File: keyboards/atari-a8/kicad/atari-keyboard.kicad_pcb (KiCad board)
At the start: 2 copper layers, 160 parts, among them J101 PLAYER 1, J102 PLAYER 2, J103 I2C DISPLAY, SW200 ESC, SW201 1, SW202 2, SW203 3, SW204 4, SW205 5, SW206 6, SW207 7, SW208 8, SW209 9, SW210 0, SW211 LT, SW212 GT, SW213 BS, SW214 C_UP, SW215 C_LEFT, SW216 C_DOWN, SW217 C_RIGHT, SW218 TAB, SW219 Q, SW220 W, SW221 E, SW222 R, SW223 T, SW224 Y, SW225 U, SW226 I, SW227 O, SW228 P, SW229 DASH, SW230 EQUAL, SW231 RETURN, SW232 HELP, SW233 RESET, SW234 OPTION, SW235 SELECT, SW236 CONTROL, SW237 A, SW238 S, SW239 D, SW240 F, SW241 G, SW242 H, SW243 J, SW244 K, SW245 L, SW246 SEMI, SW247 PLUS, SW248 ASTRIX, SW249 CAPS, SW250 START, SW251 POWER, SW252 MENU, SW253 TURBO, SW254 FN, SW255 LSHIFT, SW256 Z, SW257 X, SW258 C, SW259 V, SW260 B, SW261 N, SW262 M, SW263 COMMA, SW264 PERIOD, SW265 SLASH, SW266 RSHIFT, SW267 INV, SW268 BREAK, SW269 SPACE, U101 Elite-C

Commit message: Correct key sizes placed, diodes located, various auto-drawn stuff removed from PCB
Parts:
- removed D106: JS2_UP, keebio:Diode-dual
- removed D107: JS2_TRIG, retro-kbd:Diode-dual
- removed D108: JS2_DOWN, retro-kbd:Diode-dual
- removed D109: JS2_LEFT, retro-kbd:Diode-dual
- removed D110: JS2_RIGHT, retro-kbd:Diode-dual
- removed J102: PLAYER 2, Connector_Dsub:DSUB-9_Male_Horizontal_P2.77x2.84mm_EdgePinOffset9.90mm_Housed_MountingHolesOffset11.32mm
- SW200, SW232, SW233, SW234, SW235, SW249, SW250, SW251, SW252, SW253, SW267, SW268: footprint mx_alps:MX-1U -> mx_alps:MX-1.25U
- SW213, SW236: footprint mx_alps:MX-1U -> mx_alps:MX-2U
- SW218, SW266: footprint mx_alps:MX-1U -> mx_alps:MX-1.75U
- SW231: footprint mx_alps:MX-1U -> mx_alps:MX-1.5U
- SW255: footprint mx_alps:MX-1U -> mx_alps:MX-2.25U
- SW269: footprint mx_alps:MX-1U -> mx_alps:MX-6.25U
- moved SW250 746.5 mm to (354.8, 273.8)
- moved SW217 738.3 mm to (328.6, 276.2)
- moved SW214 735.0 mm to (309.6, 257.2)
- moved SW235 729.6 mm to (354.8, 250.0)
- moved SW234 728.4 mm to (354.8, 226.2)
- moved SW216 727.2 mm to (309.6, 276.2)
- moved SW233 727.2 mm to (354.8, 202.4)
- moved SW232 724.4 mm to (354.8, 173.8)
- moved SW215 717.0 mm to (290.5, 276.2)
- moved SW213 712.8 mm to (300.0, 200.0)
- moved SW231 702.9 mm to (304.8, 219.1)
- moved SW212 693.4 mm to (271.5, 200.0)
- moved H104 693.4 mm to (371.2, 290.3)
- moved D250 692.8 mm to (364.3, 276.2), turned to -90 degrees
- moved SW230 690.6 mm to (281.0, 219.1)
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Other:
- board outline added: 357.2 x 140.5 mm

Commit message: 3d models properly placed
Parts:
- moved D269 50.0 mm to (238.1, 280.6)
- moved D255 12.1 mm to (76.2, 261.6)
- moved D236 9.73 mm to (66.7, 242.5)
- moved D213 9.73 mm to (319.1, 204.4)
- moved D266 7.42 mm to (300.0, 261.6)
- moved D218 7.42 mm to (61.9, 223.5)
- moved D231 5.17 mm to (319.1, 223.5)
- moved D200 3.11 mm to (52.4, 204.4)
- moved D251 3.11 mm to (114.3, 178.2)
- moved D252 3.11 mm to (152.4, 178.2)
- moved D253 3.11 mm to (176.2, 178.2)
- moved D232 3.11 mm to (366.7, 178.2)
- moved D233 3.11 mm to (366.7, 206.8)
- moved D234 3.11 mm to (366.7, 230.6)
- moved D235 3.11 mm to (366.7, 254.4)
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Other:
- outline, holes or cut-outs redrawn

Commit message: All global labels rendered. MAX7219's added. PCB updaed
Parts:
- added C101: 47uF, Capacitor_THT:CP_Radial_D5.0mm_P2.50mm, F.Cu at (210.0, 173.0)
- added C102: 0.1uF, Capacitor_THT:C_Axial_L3.8mm_D2.6mm_P10.00mm_Horizontal, F.Cu at (210.0, 159.0)
- added C103: 47uF, Capacitor_THT:CP_Radial_D5.0mm_P2.50mm, F.Cu at (190.0, 173.0)
- added C104: 0.1uF, Capacitor_THT:C_Axial_L3.8mm_D2.6mm_P10.00mm_Horizontal, F.Cu at (190.0, 159.0)
- added R102: 22K, keebio:Resistor-Hybrid, F.Cu at (190.0, 183.0)
- added R103: 22K, keebio:Resistor-Hybrid, F.Cu at (210.0, 183.0)
- added U102: MAX7219, Package_DIP:DIP-24_W7.62mm_Socket_LongPads, F.Cu at (215.0, 159.0)
- added U103: MAX7219, Package_DIP:DIP-24_W7.62mm_Socket_LongPads, F.Cu at (195.0, 159.0)
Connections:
- net Net-(SW200-Pad3) renamed LED_ROW1
- net Net-(SW200-Pad4) renamed LED_COL1
- net Net-(SW201-Pad4) renamed LED_COL2
- net Net-(SW202-Pad4) renamed LED_COL3
- net Net-(SW203-Pad4) renamed LED_COL4
- net Net-(SW204-Pad4) renamed LED_COL5
- net Net-(SW205-Pad4) renamed LED_COL6
- net Net-(SW206-Pad4) renamed LED_COL7
- net Net-(SW207-Pad4) renamed LED_COL8
- net Net-(SW208-Pad4) renamed LED_COL9
- net Net-(SW209-Pad3) renamed LED_ROW2
- net Net-(SW218-Pad3) renamed LED_ROW3
- net Net-(SW227-Pad3) renamed LED_ROW4
- net Net-(SW236-Pad3) renamed LED_ROW5
- net Net-(SW245-Pad3) renamed LED_ROW6
- net Net-(SW254-Pad3) renamed LED_ROW7
- net Net-(SW263-Pad3) renamed LED_ROW8
- net Net-(SW267-Pad3) renamed LED_ROW9
- D200 pad 1: Net-(D200-K) -> SW_ROW1
- D201 pad 1: Net-(D200-K) -> SW_ROW1
- D202 pad 1: Net-(D200-K) -> SW_ROW1
- D203 pad 1: Net-(D200-K) -> SW_ROW1
- D204 pad 1: Net-(D200-K) -> SW_ROW1
- D205 pad 1: Net-(D200-K) -> SW_ROW1
- D206 pad 1: Net-(D200-K) -> SW_ROW1
- D207 pad 1: Net-(D200-K) -> SW_ROW1
- D208 pad 1: Net-(D200-K) -> SW_ROW1
- D209 pad 1: Net-(D209-K) -> SW_ROW2
- D210 pad 1: Net-(D209-K) -> SW_ROW2
- D211 pad 1: Net-(D209-K) -> SW_ROW2
- D212 pad 1: Net-(D209-K) -> SW_ROW2
- D213 pad 1: Net-(D209-K) -> SW_ROW2
- D214 pad 1: Net-(D209-K) -> SW_ROW2
- D215 pad 1: Net-(D209-K) -> SW_ROW2
- D216 pad 1: Net-(D209-K) -> SW_ROW2
- D217 pad 1: Net-(D209-K) -> SW_ROW2
- D218 pad 1: Net-(D218-K) -> SW_ROW3
- D219 pad 1: Net-(D218-K) -> SW_ROW3
- D220 pad 1: Net-(D218-K) -> SW_ROW3
- D221 pad 1: Net-(D218-K) -> SW_ROW3
- D222 pad 1: Net-(D218-K) -> SW_ROW3
- D223 pad 1: Net-(D218-K) -> SW_ROW3
- D224 pad 1: Net-(D218-K) -> SW_ROW3
- D225 pad 1: Net-(D218-K) -> SW_ROW3
- D226 pad 1: Net-(D218-K) -> SW_ROW3
- D227 pad 1: Net-(D227-K) -> SW_ROW4
- D228 pad 1: Net-(D227-K) -> SW_ROW4
- D229 pad 1: Net-(D227-K) -> SW_ROW4
- D230 pad 1: Net-(D227-K) -> SW_ROW4
- D231 pad 1: Net-(D227-K) -> SW_ROW4
- D232 pad 1: Net-(D227-K) -> SW_ROW4
- D233 pad 1: Net-(D227-K) -> SW_ROW4
- D234 pad 1: Net-(D227-K) -> SW_ROW4
- D235 pad 1: Net-(D227-K) -> SW_ROW4
- D236 pad 1: Net-(D236-K) -> SW_ROW5
- D237 pad 1: Net-(D236-K) -> SW_ROW5
- D238 pad 1: Net-(D236-K) -> SW_ROW5
- D239 pad 1: Net-(D236-K) -> SW_ROW5
- D240 pad 1: Net-(D236-K) -> SW_ROW5
- D241 pad 1: Net-(D236-K) -> SW_ROW5
- D242 pad 1: Net-(D236-K) -> SW_ROW5
- D243 pad 1: Net-(D236-K) -> SW_ROW5
- D244 pad 1: Net-(D236-K) -> SW_ROW5
- D245 pad 1: Net-(D245-K) -> SW_ROW6
- D246 pad 1: Net-(D245-K) -> SW_ROW6
- D247 pad 1: Net-(D245-K) -> SW_ROW6
- D248 pad 1: Net-(D245-K) -> SW_ROW6
- D249 pad 1: Net-(D245-K) -> SW_ROW6
- D250 pad 1: Net-(D245-K) -> SW_ROW6
- D251 pad 1: Net-(D245-K) -> SW_ROW6
- D252 pad 1: Net-(D245-K) -> SW_ROW6
- D253 pad 1: Net-(D245-K) -> SW_ROW6
- D254 pad 1: Net-(D254-K) -> SW_ROW7
- D255 pad 1: Net-(D254-K) -> SW_ROW7
- D256 pad 1: Net-(D254-K) -> SW_ROW7
- D257 pad 1: Net-(D254-K) -> SW_ROW7
- D258 pad 1: Net-(D254-K) -> SW_ROW7
- D259 pad 1: Net-(D254-K) -> SW_ROW7
- D260 pad 1: Net-(D254-K) -> SW_ROW7
- D261 pad 1: Net-(D254-K) -> SW_ROW7
- D262 pad 1: Net-(D254-K) -> SW_ROW7
- D263 pad 1: Net-(D263-K) -> SW_ROW8
- D264 pad 1: Net-(D263-K) -> SW_ROW8
- D265 pad 1: Net-(D263-K) -> SW_ROW8
- D266 pad 1: Net-(D263-K) -> SW_ROW8
- D267 pad 1: Net-(D267-K) -> SW_ROW9
- D268 pad 1: Net-(D267-K) -> SW_ROW9
- D269 pad 1: Net-(D267-K) -> SW_ROW9
- SW200 pad 2: Net-(SW200-Pad2) -> SW_COL1
- SW201 pad 2: Net-(SW201-Pad2) -> SW_COL2
- SW202 pad 2: Net-(SW202-Pad2) -> SW_COL3
- SW203 pad 2: Net-(SW203-Pad2) -> SW_COL4
- SW204 pad 2: Net-(SW204-Pad2) -> SW_COL5
- SW205 pad 2: Net-(SW205-Pad2) -> SW_COL6
- SW206 pad 2: Net-(SW206-Pad2) -> SW_COL7
- SW207 pad 2: Net-(SW207-Pad2) -> SW_COL8
- SW208 pad 2: Net-(SW208-Pad2) -> SW_COL9
- SW209 pad 2: Net-(SW200-Pad2) -> SW_COL1
- SW210 pad 2: Net-(SW201-Pad2) -> SW_COL2
- SW211 pad 2: Net-(SW202-Pad2) -> SW_COL3
- SW212 pad 2: Net-(SW203-Pad2) -> SW_COL4
- SW213 pad 2: Net-(SW204-Pad2) -> SW_COL5
- SW214 pad 2: Net-(SW205-Pad2) -> SW_COL6
- SW215 pad 2: Net-(SW206-Pad2) -> SW_COL7
- SW216 pad 2: Net-(SW207-Pad2) -> SW_COL8
- SW217 pad 2: Net-(SW208-Pad2) -> SW_COL9
- SW218 pad 2: Net-(SW200-Pad2) -> SW_COL1
- SW219 pad 2: Net-(SW201-Pad2) -> SW_COL2
- SW220 pad 2: Net-(SW202-Pad2) -> SW_COL3
- SW221 pad 2: Net-(SW203-Pad2) -> SW_COL4
- SW222 pad 2: Net-(SW204-Pad2) -> SW_COL5
- SW223 pad 2: Net-(SW205-Pad2) -> SW_COL6
- SW224 pad 2: Net-(SW206-Pad2) -> SW_COL7
- SW225 pad 2: Net-(SW207-Pad2) -> SW_COL8
- SW226 pad 2: Net-(SW208-Pad2) -> SW_COL9
- SW227 pad 2: Net-(SW200-Pad2) -> SW_COL1
- SW228 pad 2: Net-(SW201-Pad2) -> SW_COL2
- SW229 pad 2: Net-(SW202-Pad2) -> SW_COL3
- SW230 pad 2: Net-(SW203-Pad2) -> SW_COL4
- SW231 pad 2: Net-(SW204-Pad2) -> SW_COL5
- SW232 pad 2: Net-(SW205-Pad2) -> SW_COL6
- SW233 pad 2: Net-(SW206-Pad2) -> SW_COL7
- SW234 pad 2: Net-(SW207-Pad2) -> SW_COL8
- SW235 pad 2: Net-(SW208-Pad2) -> SW_COL9
- SW236 pad 2: Net-(SW200-Pad2) -> SW_COL1
- SW237 pad 2: Net-(SW201-Pad2) -> SW_COL2
- SW238 pad 2: Net-(SW202-Pad2) -> SW_COL3
- SW239 pad 2: Net-(SW203-Pad2) -> SW_COL4
- SW240 pad 2: Net-(SW204-Pad2) -> SW_COL5
- SW241 pad 2: Net-(SW205-Pad2) -> SW_COL6
- SW242 pad 2: Net-(SW206-Pad2) -> SW_COL7
- SW243 pad 2: Net-(SW207-Pad2) -> SW_COL8
- SW244 pad 2: Net-(SW208-Pad2) -> SW_COL9
- SW245 pad 2: Net-(SW200-Pad2) -> SW_COL1
- SW246 pad 2: Net-(SW201-Pad2) -> SW_COL2
- SW247 pad 2: Net-(SW202-Pad2) -> SW_COL3
- SW248 pad 2: Net-(SW203-Pad2) -> SW_COL4
- SW249 pad 2: Net-(SW204-Pad2) -> SW_COL5
- SW250 pad 2: Net-(SW205-Pad2) -> SW_COL6
- SW251 pad 2: Net-(SW206-Pad2) -> SW_COL7
- SW252 pad 2: Net-(SW207-Pad2) -> SW_COL8
- SW253 pad 2: Net-(SW208-Pad2) -> SW_COL9
- SW254 pad 2: Net-(SW200-Pad2) -> SW_COL1
- SW255 pad 2: Net-(SW201-Pad2) -> SW_COL2
- SW256 pad 2: Net-(SW202-Pad2) -> SW_COL3
- SW257 pad 2: Net-(SW203-Pad2) -> SW_COL4
- SW258 pad 2: Net-(SW204-Pad2) -> SW_COL5
- SW259 pad 2: Net-(SW205-Pad2) -> SW_COL6
- SW260 pad 2: Net-(SW206-Pad2) -> SW_COL7
- SW261 pad 2: Net-(SW207-Pad2) -> SW_COL8
- SW262 pad 2: Net-(SW208-Pad2) -> SW_COL9
- SW263 pad 2: Net-(SW205-Pad2) -> SW_COL6
- SW264 pad 2: Net-(SW206-Pad2) -> SW_COL7
- SW265 pad 2: Net-(SW207-Pad2) -> SW_COL8
- SW266 pad 2: Net-(SW208-Pad2) -> SW_COL9
- SW267 pad 2: Net-(SW205-Pad2) -> SW_COL6
- SW268 pad 2: Net-(SW206-Pad2) -> SW_COL7
- SW269 pad 2: Net-(SW207-Pad2) -> SW_COL8
- U101 pad 10: R4 -> SW_ROW4
- U101 pad 11: R5 -> SW_ROW5
- U101 pad 12: R6 -> SW_ROW6
- U101 pad 13: C8 -> SW_COL8
- U101 pad 14: C7 -> SW_COL7
- U101 pad 15: C6 -> SW_COL6
- U101 pad 16: C5 -> SW_COL5
- U101 pad 17: C4 -> SW_COL4
- U101 pad 18: C3 -> SW_COL3
- U101 pad 19: C2 -> SW_COL2
- U101 pad 20: C1 -> SW_COL1
- U101 pad 25: R7 -> SW_ROW7
- U101 pad 26: R8 -> SW_ROW8
- U101 pad 27: R9 -> SW_ROW9
- U101 pad 29: C9 -> SW_COL9
- U101 pad 7: R1 -> SW_ROW1
- U101 pad 8: R2 -> SW_ROW2
- U101 pad 9: R3 -> SW_ROW3
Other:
- outline, holes or cut-outs redrawn

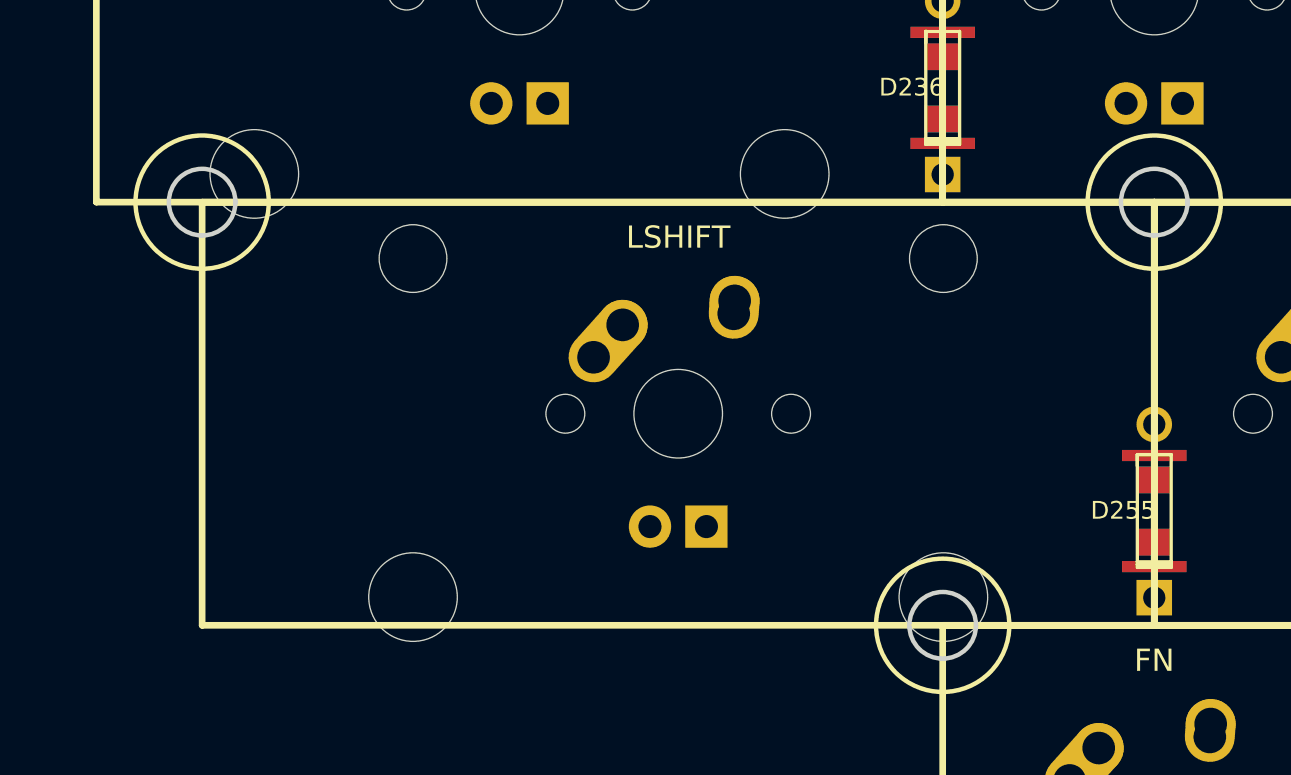
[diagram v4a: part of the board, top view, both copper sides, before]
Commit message: Changed LSHIFT from 2.25U to 2U (more available)
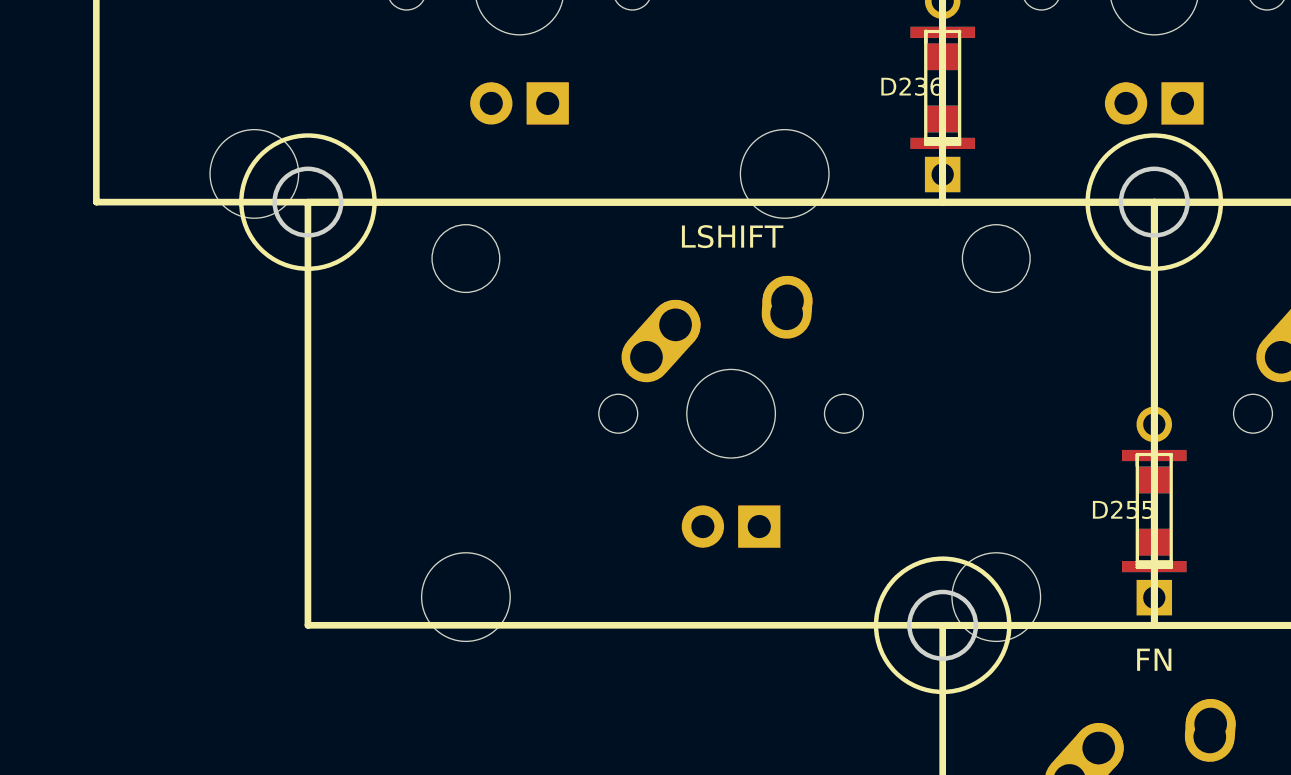
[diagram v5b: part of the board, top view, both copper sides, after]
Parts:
- SW255: footprint mx_alps:MX-2.25U -> mx_alps:MX-2U
- moved SW255 2.38 mm to (57.1, 257.2)
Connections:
- U101 pad 28: unconnected-(U101-F1-Pad28) -> /SPI_LOAD
- U102 pad 12: SW_COL7 -> /SPI_LOAD
- U103 pad 12: SW_COL7 -> /SPI_LOAD
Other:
- outline, holes or cut-outs redrawn
